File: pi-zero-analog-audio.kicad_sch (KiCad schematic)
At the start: 19 parts, among them J1 GPIO, J2 SJ1-3555NG-BE, J3 Screw_Terminal_01x04, U1 LP5907MFX-3.3, U2 74LVC2G34

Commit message: Evenings come with the same regularity as the mornings
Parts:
- removed J3: Screw_Terminal_01x04, TerminalBlock:TerminalBlock_bornier-4_P5.08mm, symbol Connector:Screw_Terminal_01x04
- C3, C6, C8: symbol Device:C_Polarized -> Device:C
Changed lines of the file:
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@@
-    (stroke (width 0) (type default) (color 0 0 0 0))
-  )
-  (wire (pts (xy 111.76 41.91) (xy 111.76 49.53))
     (stroke (width 0) (type default) (color 0 0 0 0))
   )
@@
   )
   (label "AUDIO_R" (at 175.26 52.07 0)
-    (effects (font (size 1.27 1.27)) (justify left bottom))
-  )
-  (label "AUD_3V3" (at 111.76 41.91 0)
     (effects (font (size 1.27 1.27)) (justify left bottom))
   )
@@
     (pin "9")
   )
-  (symbol (lib_id "Device:C_Polarized") (at 57.15 63.5 0) (unit 1)
+  (symbol (lib_id "Device:C") (at 57.15 63.5 0) (unit 1)
     (in_bom yes) (on_board yes) (fields_autoplaced)
     (property "Reference" "C8" (id 0) (at 60.071 61.7763 0)
@@
   )
   (symbol (lib_id "SJ1-3555NG-BE:SJ1-3555NG-BE") (at 203.2 36.83 180) (unit 1)
-    (in_bom yes) (on_board yes) (fields_autoplaced)
-    (property "Reference" "J2" (id 0) (at 211.582 35.9953 0)
+    (in_bom yes) (on_board yes)
+    (property "Reference" "J2" (id 0) (at 201.93 25.4 0)
       (effects (font (size 1.27 1.27)) (justify right))
     )
-    (property "Value" "SJ1-3555NG-BE" (id 1) (at 211.582 38.5322 0)
+    (property "Value" "SJ1-3555NG-BE" (id 1) (at 195.58 27.94 0)
       (effects (font (size 1.27 1.27)) (justify right))
     )
@@
     (pin "1")
   )
-  (symbol (lib_id "Device:C_Polarized") (at 157.48 52.07 90) (unit 1)
+  (symbol (lib_id "Device:C") (at 157.48 52.07 90) (unit 1)
     (in_bom yes) (on_board yes) (fields_autoplaced)
     (property "Reference" "C6" (id 0) (at 156.591 46.2112 90))
@@
     (pin "1")
   )
-  (symbol (lib_id "Device:C_Polarized") (at 157.48 27.94 90) (unit 1)
+  (symbol (lib_id "Device:C") (at 157.48 27.94 90) (unit 1)
     (in_bom yes) (on_board yes) (fields_autoplaced)
     (property "Reference" "C3" (id 0) (at 156.591 22.0812 90))
@@
     (pin "1")
   )
-  (symbol (lib_id "Connector:Screw_Terminal_01x04") (at 186.69 124.46 0) (unit 1)
-    (in_bom yes) (on_board yes) (fields_autoplaced)
-    (property "Reference" "J3" (id 0) (at 188.722 124.8953 0)
-      (effects (font (size 1.27 1.27)) (justify left))
-    )
-    (property "Value" "Screw_Terminal_01x04" (id 1) (at 188.722 127.4322 0)
-      (effects (font (size 1.27 1.27)) (justify left))
-    )
-    (property "Footprint" "TerminalBlock:TerminalBlock_bornier-4_P5.08mm" (id 2) (at 186.69 124.46 0)
-      (effects (font (size 1.27 1.27)) hide)
-    )
-    (property "Datasheet" "~" (id 3) (at 186.69 124.46 0)
-      (effects (font (size 1.27 1.27)) hide)
-    )
-    (pin "1")
-    (pin "2")
-    (pin "3")
-    (pin "4")
-  )
-  (symbol (lib_id "power:GND") (at 111.76 54.61 0) (unit 1)
-    (in_bom yes) (on_board yes) (fields_autoplaced)
-    (property "Reference" "#PWR014" (id 0) (at 111.76 60.96 0)
-      (effects (font (size 1.27 1.27)) hide)
-    )
-    (property "Value" "GND" (id 1) (at 111.76 59.0534 0))
-    (property "Footprint" "" (id 2) (at 111.76 54.61 0)
-      (effects (font (size 1.27 1.27)) hide)
-    )
-    (property "Datasheet" "" (id 3) (at 111.76 54.61 0)
-      (effects (font (size 1.27 1.27)) hide)
-    )
-    (pin "1")
-  )
   (symbol (lib_id "power:GND") (at 121.92 38.1 0) (unit 1)
     (in_bom yes) (on_board yes) (fields_autoplaced)
@@
       (reference "#PWR013") (unit 1) (value "GND") (footprint "")
     )
-    (path "/e6b8cf73-a12e-464f-9ef7-24d6593fda44"
-      (reference "#PWR014") (unit 1) (value "GND") (footprint "")
-    )
     (path "/a31e2c62-695d-402d-aace-8193a0330673"
       (reference "#PWR015") (unit 1) (value "GND") (footprint "")
@@
       (reference "J2") (unit 1) (value "SJ1-3555NG-BE") (footprint "library:CUI_SJ1-3555NG-BE")
     )
-    (path "/e4e0ca7e-6acb-48b6-bf2b-4d2939783b7f"
-      (reference "J3") (unit 1) (value "Screw_Terminal_01x04") (footprint "TerminalBlock:TerminalBlock_bornier-4_P5.08mm")
-    )
     (path "/72d935ce-432c-4183-b481-300609728f6c"

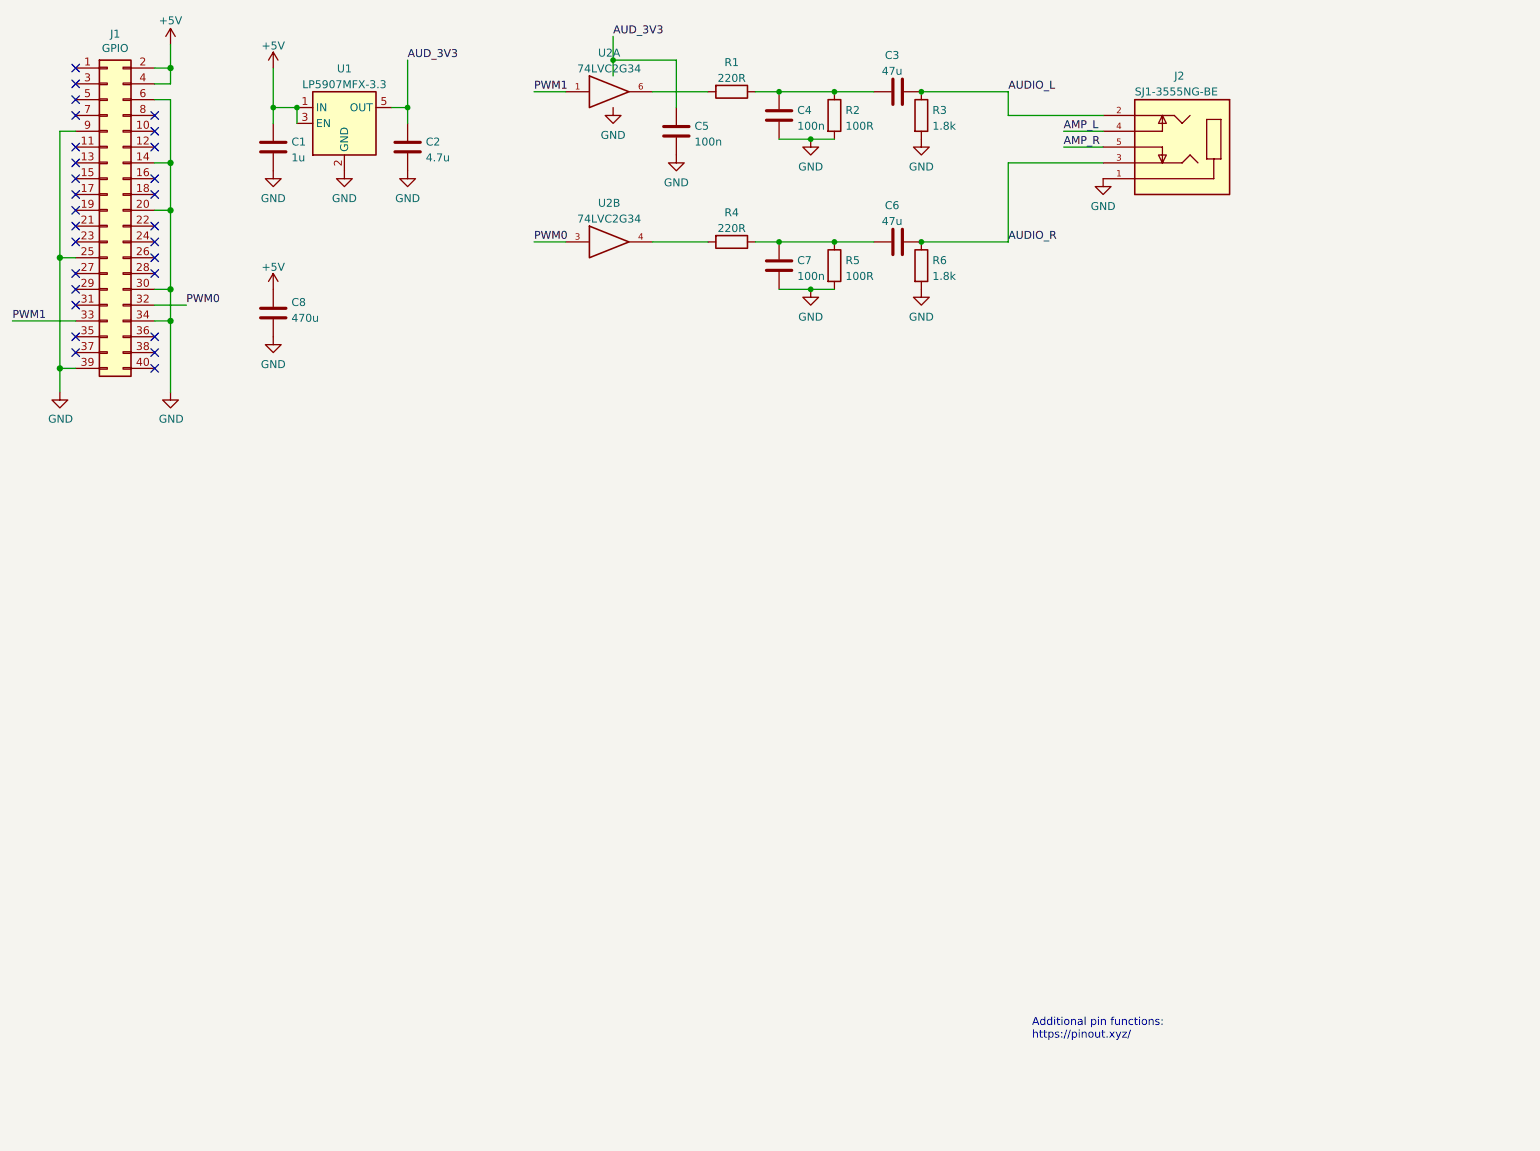
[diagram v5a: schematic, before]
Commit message: Adding PAM8403D based amplifier
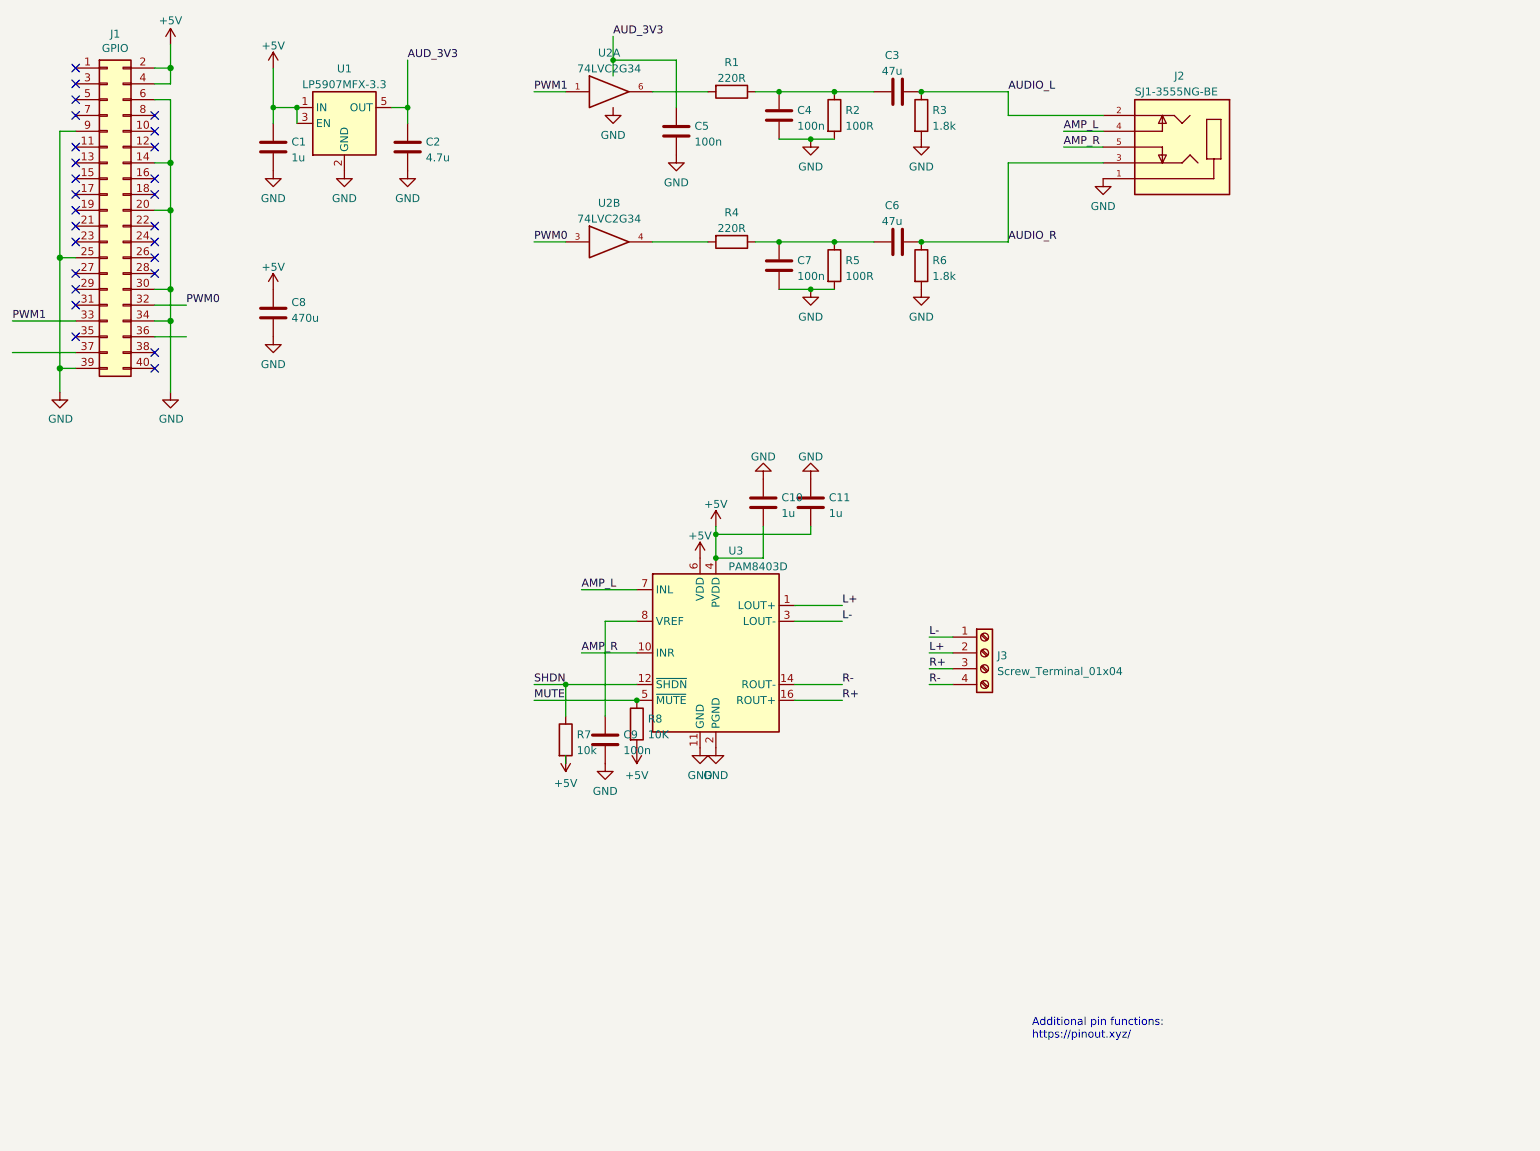
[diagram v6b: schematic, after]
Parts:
- added C10, C11: 1u, Capacitor_SMD:C_0805_2012Metric_Pad1.18x1.45mm_HandSolder, symbol Device:C
- added C9: 100n, Capacitor_SMD:C_0805_2012Metric_Pad1.18x1.45mm_HandSolder, symbol Device:C
- added J3: Screw_Terminal_01x04, TerminalBlock:TerminalBlock_bornier-4_P5.08mm, symbol Connector:Screw_Terminal_01x04
- added R7: 10k, Resistor_SMD:R_0805_2012Metric_Pad1.20x1.40mm_HandSolder, symbol Device:R
- added R8: 10K, Resistor_SMD:R_0805_2012Metric_Pad1.20x1.40mm_HandSolder, symbol Device:R
- added U3: PAM8403D, Package_SO:SOP-16_3.9x9.9mm_P1.27mm, symbol Amplifier_Audio:PAM8403D
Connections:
- net +5V: now also C10.2, C11.2, R7.2, R8.2, U3.13 (PVDD), U3.4 (PVDD), U3.6 (VDD)
- net AMP_L: now also U3.7 (INL)
- net AMP_R: now also U3.10 (INR)
- net GND: now also C10.1, C11.1, C9.2, U3.11 (GND), U3.15 (PGND), U3.2 (PGND)
- new net: C9.1, U3.8 (VREF)
- new net L+: J3.2 (Pin_2), U3.1 (LOUT+)
- new net L-: J3.1 (Pin_1), U3.3 (LOUT-)
- new net MUTE: R8.1, U3.5 (~{MUTE})
- new net R+: J3.3 (Pin_3), U3.16 (ROUT+)
- new net R-: J3.4 (Pin_4), U3.14 (ROUT-)
- new net SHDN: R7.1, U3.12 (~{SHDN})
- no-connect marks 28 -> 26

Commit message: Some more clearance of zone fixes
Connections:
- net MUTE: now also J1.36 (Pin_36)
- net SHDN: now also J1.37 (Pin_37)
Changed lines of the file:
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@@
+    (effects (font (size 1.27 1.27)) (justify left bottom))
+  )
+  (label "MUTE" (at 43.18 67.31 0)
     (effects (font (size 1.27 1.27)) (justify left bottom))
   )
@@
     (effects (font (size 1.27 1.27)) (justify left bottom))
   )
+  (label "SHDN" (at 15.24 69.85 0)
+    (effects (font (size 1.27 1.27)) (justify left bottom))
+  )

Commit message: minor cleanup
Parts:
- C8: symbol Device:C -> Device:C_Polarized
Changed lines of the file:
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@@
     (pin "9")
   )
-  (symbol (lib_id "Device:C") (at 57.15 63.5 0) (unit 1)
+  (symbol (lib_id "Device:C_Polarized") (at 57.15 63.5 0) (unit 1)
     (in_bom yes) (on_board yes) (fields_autoplaced)
     (property "Reference" "C8" (id 0) (at 60.071 61.7763 0)
